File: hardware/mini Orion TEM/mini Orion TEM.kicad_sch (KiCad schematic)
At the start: 85 parts, among them J101 HRLV, J102 bridge to bottom board, J103 SWD, J104 fan pwr source, J105 VT harness, J106 fan PWR, J2 Fan enable, Q101 DI035P04PT, SW101 SW_DIP_x06, U101 ISOM8110DFS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

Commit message: instructions for dinguses
you know who
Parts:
- C101: value 1u -> 10u; mouser https://www.mouser.com/ProductDetail/Samsung-Electro-Mechanics/CL31B105KCHNNNE?qs=349EhDEZ59qH1i3RhF2lug%3D%3D -> https://www.mouser.com/ProductDetail/Samsung-Electro-Mechanics/CL31A106KBHNNNE?qs=sGAEpiMZZMsh%252B1woXyUXjxqcB7t9naYpzWmpMbMJIKQ%3D; specs 1uF, 100VDC, X7R, 10%, -55C, +125C -> 10uF, 50VDC, X5R, 10%, -55C, +85C; unit x1 0.15 -> (none); unit x10 0.061 -> 0.07
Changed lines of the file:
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@@
+	)
+	(symbol
+		(lib_id "Device:C_Small")
+		(at 73.66 39.37 0)
+		(unit 1)
+		(exclude_from_sim no)
+		(in_bom yes)
+		(on_board yes)
+		(dnp no)
+		(property "Reference" "C101"
+			(at 76.2 38.1062 0)
+			(effects
+				(font
+					(size 1.27 1.27)
+				)
+				(justify left)
+			)
+		)
+		(property "Value" "10u"
+			(at 76.2 40.6462 0)
+			(effects
+				(font
+					(size 1.27 1.27)
+				)
+				(justify left)
+			)
+		)
+		(property "Footprint" "Capacitor_SMD:C_1206_3216Metric_Pad1.33x1.80mm_HandSolder"
+			(at 73.66 39.37 0)
+			(effects
+				(font
+					(size 1.27 1.27)
+				)
+				(hide yes)
+			)
+		)
+		(property "Datasheet" ""
+			(at 73.66 39.37 0)
+			(effects
+				(font
+					(size 1.27 1.27)
+				)
+				(hide yes)
+			)
+		)
+		(property "Description" ""
+			(at 73.66 39.37 0)
+			(effects
+				(font
+					(size 1.27 1.27)
+				)
+				(hide yes)
+			)
+		)
+		(property "Sim.Device" ""
+			(at 73.66 39.37 0)
+			(effects
+				(font
+					(size 1.27 1.27)
+				)
+				(hide yes)
+			)
+		)
+		(property "Sim.Type" ""
+			(at 73.66 39.37 0)
+			(effects
+				(font
+					(size 1.27 1.27)
+				)
+				(hide yes)
+			)
+		)
+		(property "mouser" "https://www.mouser.com/ProductDetail/Samsung-Electro-Mechanics/CL31A106KBHNNNE?qs=sGAEpiMZZMsh%252B1woXyUXjxqcB7t9naYpzWmpMbMJIKQ%3D"
+			(at 73.66 39.37 0)
+			(effects
+				(font
+					(size 1.27 1.27)
+				)
+				(hide yes)
+			)
+		)
+		(property "specs" "10uF, 50VDC, X5R, 10%, -55C, +85C"
+			(at 73.66 39.37 0)
+			(effects
+				(font
+					(size 1.27 1.27)
+				)
+				(hide yes)
+			)
+		)
+		(property "unit x10" "0.07"
+			(at 73.66 39.37 0)
+			(effects
+				(font
+					(size 1.27 1.27)
+				)
+				(hide yes)
+			)
+		)
+		(property "Sim.Pins" ""
+			(at 73.66 39.37 0)
+			(effects
+				(font
+					(size 1.27 1.27)
+				)
+				(hide yes)
+			)
+		)
+		(property "note" ""
+			(at 73.66 39.37 0)
+			(effects
+				(font
+					(size 1.27 1.27)
+				)
+				(hide yes)
+			)
+		)
+		(pin "2"
+		)
+		(pin "1"
+		)
+		(instances
+			(project "mini Orion TEM"
+				(path "/b084770c-fa69-4b11-9ca5-6e8bd0701598"
+					(reference "C101")
+					(unit 1)
+				)
+			)
+		)
 	)
 	(symbol
@@
 					(unit 1)
 				)
-			)
-		)
-	)
-	(symbol
-		(lib_id "Device:C_Small")
-		(at 73.66 39.37 0)
-		(unit 1)
-		(exclude_from_sim no)
-		(in_bom yes)
-		(on_board yes)
-		(dnp no)
-		(property "Reference" "C101"
-			(at 76.2 38.1062 0)
-			(effects
-				(font
-					(size 1.27 1.27)
-				)
-				(justify left)
-			)
-		)
-		(property "Value" "1u"
-			(at 76.2 40.6462 0)
-			(effects
-				(font
-					(size 1.27 1.27)
-				)
-				(justify left)
-			)
-		)
-		(property "Footprint" "Capacitor_SMD:C_1206_3216Metric_Pad1.33x1.80mm_HandSolder"
-			(at 73.66 39.37 0)
-			(effects
-				(font
-					(size 1.27 1.27)
-				)
-				(hide yes)
-			)
-		)
-		(property "Datasheet" ""
-			(at 73.66 39.37 0)
-			(effects
-				(font
-					(size 1.27 1.27)
-				)
-				(hide yes)
-			)
-		)
-		(property "Description" ""
-			(at 73.66 39.37 0)
-			(effects
-				(font
-					(size 1.27 1.27)
-				)
-				(hide yes)
-			)
-		)
-		(property "Sim.Device" ""
-			(at 73.66 39.37 0)
-			(effects
-				(font
-					(size 1.27 1.27)
-				)
-				(hide yes)
-			)
-		)
-		(property "Sim.Type" ""
-			(at 73.66 39.37 0)
-			(effects
-				(font
-					(size 1.27 1.27)
-				)
-				(hide yes)
-			)
-		)
-		(property "mouser" "https://www.mouser.com/ProductDetail/Samsung-Electro-Mechanics/CL31B105KCHNNNE?qs=349EhDEZ59qH1i3RhF2lug%3D%3D"
-			(at 73.66 39.37 0)
-			(effects
-				(font
-					(size 1.27 1.27)
-				)
-				(hide yes)
-			)
-		)
-		(property "specs" "1uF, 100VDC, X7R, 10%, -55C, +125C"
-			(at 73.66 39.37 0)
-			(effects
-				(font
-					(size 1.27 1.27)
-				)
-				(hide yes)
-			)
-		)
-		(property "unit x10" "0.061"
-			(at 73.66 39.37 0)
-			(effects
-				(font
-					(size 1.27 1.27)
-				)
-				(hide yes)
-			)
-		)
-		(property "Sim.Pins" ""
-			(at 73.66 39.37 0)
-			(effects
-				(font
-					(size 1.27 1.27)
-				)
-				(hide yes)
-			)
-		)
-		(property "note" ""
-			(at 73.66 39.37 0)
-			(effects
-				(font
-					(size 1.27 1.27)
-				)
-				(hide yes)
-			)
-		)
-		(property "unit x1" "0.15"
-			(at 73.66 39.37 0)
-			(effects
-				(font
-					(size 1.27 1.27)
-				)
-				(hide yes)
-			)
-		)
-		(property "Mouser Part Number" ""
-			(at 73.66 39.37 0)
-			(effects
-				(font
-					(size 1.27 1.27)
-				)
-				(hide yes)
-			)
-		)
-		(pin "2"
-		)
-		(pin "1"
-		)
-		(instances
-			(project "mini Orion TEM"
-				(path "/b084770c-fa69-4b11-9ca5-6e8bd0701598"
-					(reference "C101")
-					(unit 1)
-				)

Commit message: rounder gooder
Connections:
- net HRLV_CAN+: now also FL101.4; no longer FL101.1
- net HRLV_CAN-: now also FL101.1; no longer FL101.4
- net at FL101.2: now also U104.5 (CANL); no longer U104.6 (CANH)
- net at FL101.3: now also U104.6 (CANH); no longer U104.5 (CANL)
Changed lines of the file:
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@@
 		(lib_id "Filter:Choke_CommonMode_FerriteCore_1243")
 		(at 104.14 54.61 0)
+		(mirror x)
 		(unit 1)
 		(exclude_from_sim no)
@@
 		(dnp no)
 		(property "Reference" "FL101"
-			(at 104.14 49.53 0)
+			(at 104.14 49.784 0)
 			(effects
 				(font
@@
 		)
 		(property "Value" "Choke_CommonMode_FerriteCore_1243"
-			(at 104.013 49.53 0)
+			(at 104.013 59.69 0)
 			(effects
 				(font
@@
 		)
 		(property "Footprint" "Inductor_SMD:L_CommonModeChoke_Coilcraft_1812CAN"
-			(at 104.14 60.96 0)
+			(at 104.14 48.26 0)
 			(effects
 				(font
@@
 		)
 		(property "Datasheet" "~"
-			(at 104.14 62.865 0)
+			(at 104.14 46.355 0)
 			(effects
 				(font
@@
 		)
 		(property "Description" "EMI 2-inductor common mode filter"
-			(at 108.204 55.372 0)
+			(at 108.204 53.848 0)
 			(effects
 				(font

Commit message: human part checker
always the part. never the part.
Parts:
- added Q102: MMBT5550L, Package_TO_SOT_SMD:SOT-23, symbol Transistor_BJT:MMBT5550L
- R113, R114: value 88.7k -> 40.2k; mouser https://www.mouser.com/ProductDetail/YAGEO/AC0805FR-0788K7L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 -> https://www.mouser.com/ProductDetail/KOA-Speer/RK73H2ATTD40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; specs 88.7kR, 125mW, 150V, 100ppm, 1%, -55C, +155C -> 40.2k ohm, 250mW, 1%, 150V, 100ppm, -55C, +155C; unit x1 0.01 -> 0.1; unit x10 0.011 -> 0.02
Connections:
- net +3V3: now also Q102.3 (C)
- net LV_FAN_PWM: now also Q102.1 (B); no longer R102.1
- new net: Q102.2 (E), R102.1
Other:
- note added: "join with external wire. see info.md in project folder"
- note added: "trust-me-bro technology"
- note removed: "join with external wire"
- moved on the sheet: C109, C110, C113, C114, R102

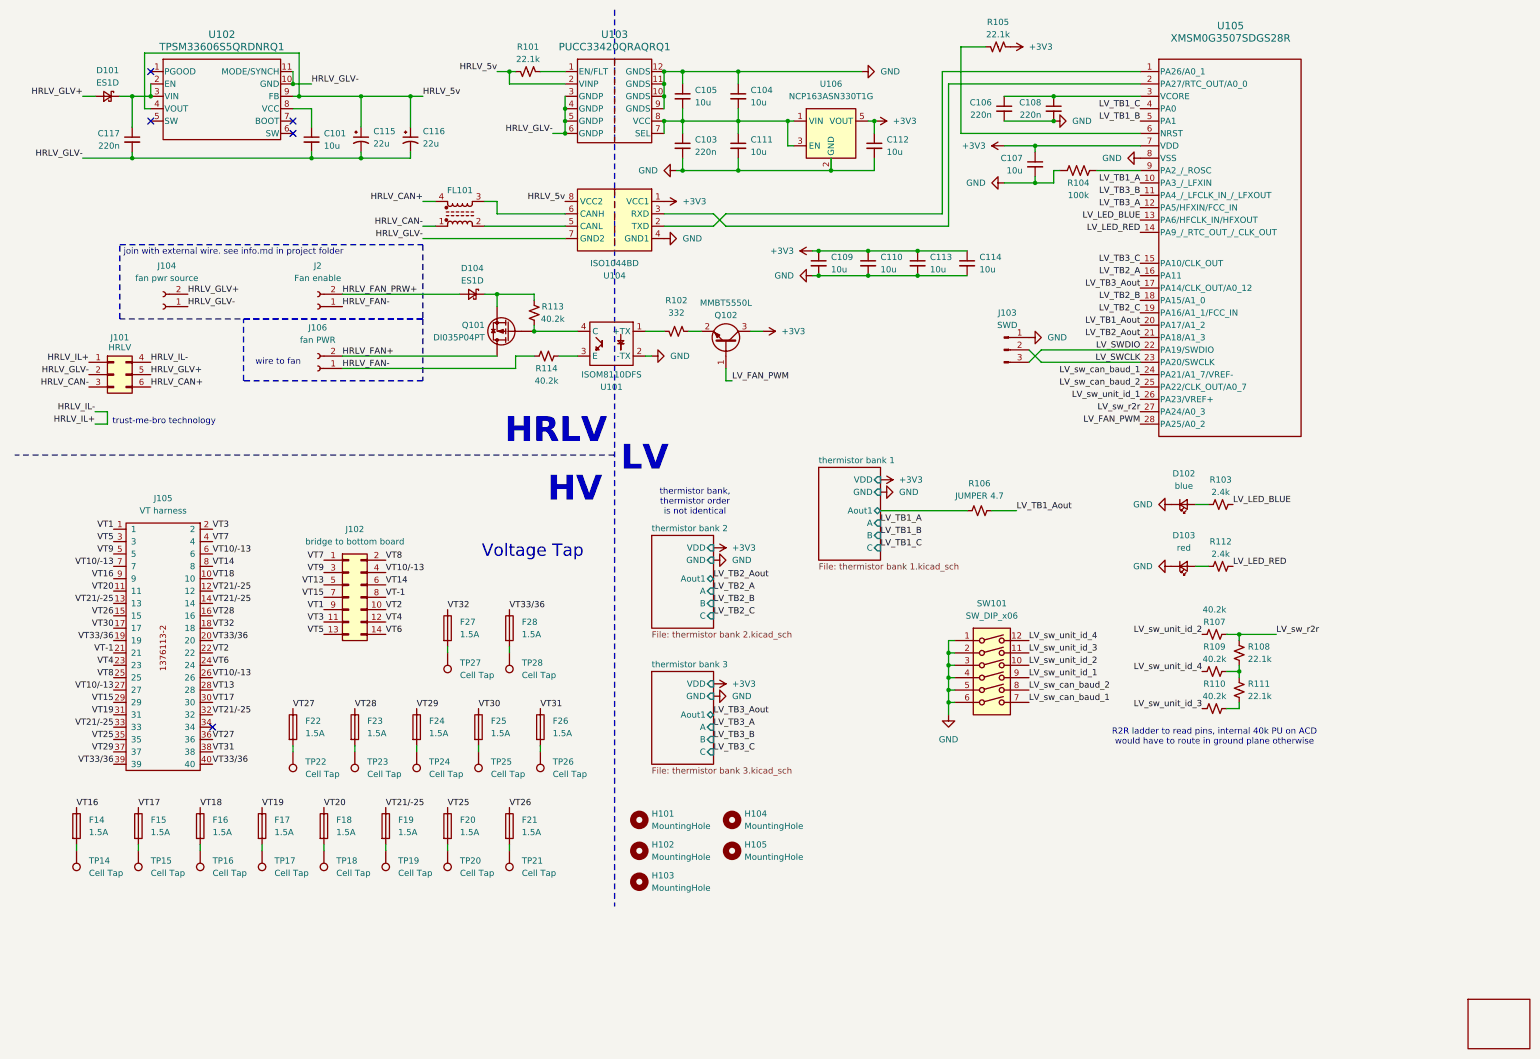
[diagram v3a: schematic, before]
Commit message: fixed silkscreen dissipearing
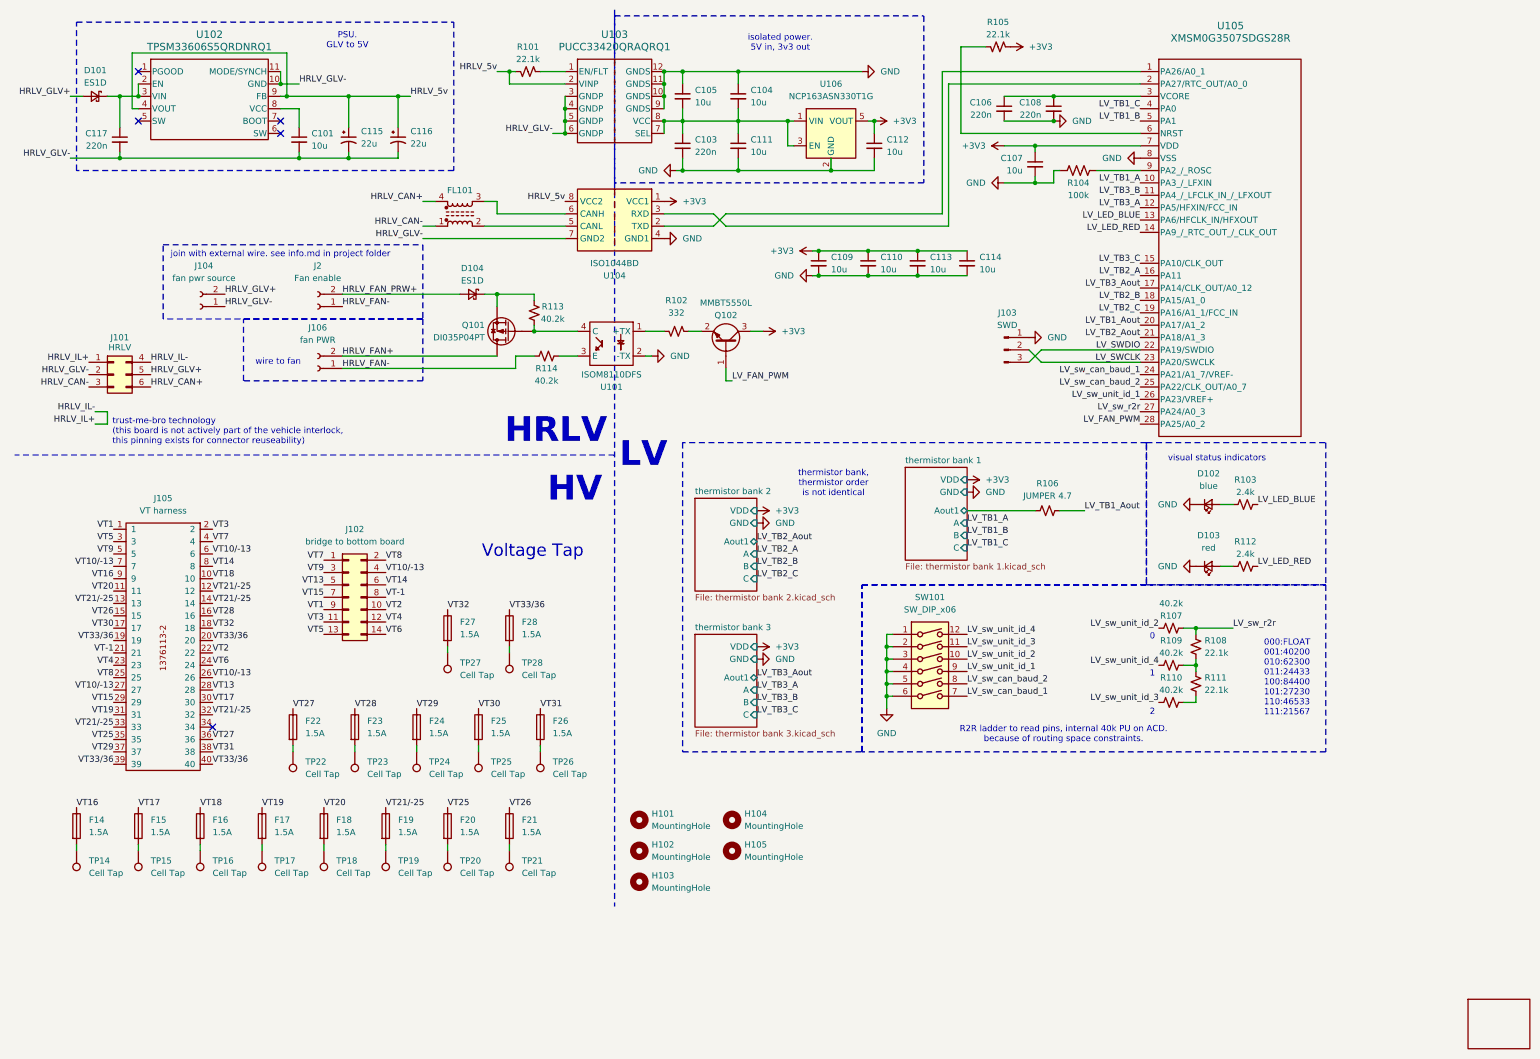
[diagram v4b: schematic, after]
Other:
- note added: "0"
- note added: "000:FLOAT 001:40200 010:62300 011:24433 100:84400 101:27230 110:46533 111:21567"
- note added: "1"
- note added: "2"
- note added: "PSU. GLV to 5V"
- note added: "R2R ladder to read pins, internal 40k PU on ACD. because of routing space constraints."
- note added: "isolated power. 5V in, 3v3 out"
- note added: "trust-me-bro technology (this board is not actively part of the vehicle interlock, this pinning exists for connector reuseability)"
- note added: "visual status indicators"
- note removed: "R2R ladder to read pins, internal 40k PU on ACD would have to route in ground plane otherwise"
- note removed: "trust-me-bro technology"
- moved on the sheet: C101, C115, C116, C117, D101, D102, D103, J104, R103, R106, R107, R108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

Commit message: maby
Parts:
- removed C115, C116: 22u, Capacitor_SMD:C_0805_2012Metric_Pad1.18x1.45mm_HandSolder, symbol Device:C_Polarized_Small_US
- added C115, C116: 22u, Capacitor_SMD:C_0805_2012Metric_Pad1.18x1.45mm_HandSolder, symbol Device:C_Small
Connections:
- net HRLV_5v: now also C115.1, C116.1
- net HRLV_GLV-: now also C115.2, C116.2
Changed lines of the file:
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@@
 	)
 	(symbol
+		(lib_id "Device:C_Small")
+		(at 81.28 39.37 0)
+		(unit 1)
+		(exclude_from_sim no)
+		(in_bom yes)
+		(on_board yes)
+		(dnp no)
+		(property "Reference" "C115"
+			(at 83.82 38.1062 0)
+			(effects
+				(font
+					(size 1.27 1.27)
+				)
+				(justify left)
+			)
+		)
+		(property "Value" "22u"
+			(at 83.82 40.6462 0)
+			(effects
+				(font
+					(size 1.27 1.27)
+				)
+				(justify left)
+			)
+		)
+		(property "Footprint" "Capacitor_SMD:C_0805_2012Metric_Pad1.18x1.45mm_HandSolder"
+			(at 81.28 39.37 0)
+			(effects
+				(font
+					(size 1.27 1.27)
+				)
+				(hide yes)
+			)
+		)
+		(property "Datasheet" ""
+			(at 81.28 39.37 0)
+			(effects
+				(font
+					(size 1.27 1.27)
+				)
+				(hide yes)
+			)
+		)
+		(property "Description" ""
+			(at 81.28 39.37 0)
+			(effects
+				(font
+					(size 1.27 1.27)
+				)
+				(hide yes)
+			)
+		)
+		(property "mouser" "https://www.mouser.com/ProductDetail/Samsung-Electro-Mechanics/CL21A226MAYNNNE?qs=sGAEpiMZZMsh%252B1woXyUXj9e2R%2FOkAO5o4FNiyGuFzx8%3D"
+			(at 81.28 39.37 0)
+			(effects
+				(font
+					(size 1.27 1.27)
+				)
+				(hide yes)
+			)
+		)
+		(property "specs" "22uF, 25V, 20%, X5R, -55C, +85C, mlcc"
+			(at 81.28 39.37 0)
+			(effects
+				(font
+					(size 1.27 1.27)
+				)
+				(hide yes)
+			)
+		)
+		(property "unit x10" "0.043"
+			(at 81.28 39.37 0)
+			(effects
+				(font
+					(size 1.27 1.27)
+				)
+				(hide yes)
+			)
+		)
+		(pin "2"
+		)
+		(pin "1"
+		)
+		(instances
+			(project "mini Orion TEM"
+				(path "/b084770c-fa69-4b11-9ca5-6e8bd0701598"
+					(reference "C115")
+					(unit 1)
+				)
+			)
+		)
+	)
+	(symbol
 		(lib_id "power:+3V3")
 		(at 217.17 20.32 270)
@@
 	)
 	(symbol
-		(lib_id "Device:C_Polarized_Small_US")
-		(at 91.44 39.37 0)
-		(unit 1)
-		(exclude_from_sim no)
-		(in_bom yes)
-		(on_board yes)
-		(dnp no)
-		(property "Reference" "C116"
-			(at 93.98 37.6681 0)
-			(effects
-				(font
-					(size 1.27 1.27)
-				)
-				(justify left)
-			)
-		)
-		(property "Value" "22u"
-			(at 93.98 40.2081 0)
-			(effects
-				(font
-					(size 1.27 1.27)
-				)
-				(justify left)
-			)
-		)
-		(property "Footprint" "Capacitor_SMD:C_0805_2012Metric_Pad1.18x1.45mm_HandSolder"
-			(at 91.44 39.37 0)
-			(effects
-				(font
-					(size 1.27 1.27)
-				)
-				(hide yes)
-			)
-		)
-		(property "Datasheet" "~"
-			(at 91.44 39.37 0)
-			(effects
-				(font
-					(size 1.27 1.27)
-				)
-				(hide yes)
-			)
-		)
-		(property "Description" "tantalium. 7v"
-			(at 91.44 39.37 0)
-			(effects
-				(font
-					(size 1.27 1.27)
-				)
-				(hide yes)
-			)
-		)
-		(property "mouser" "https://www.mouser.com/ProductDetail/Vishay-Sprague/TMCP0J226MTRF?qs=sGAEpiMZZMtZ1n0r9vR22SXwTtNEhYRLx5RUlLXY%252BB2j8IDJMMLmhQ%3D%3D"
-			(at 91.44 39.37 0)
-			(effects
-				(font
-					(size 1.27 1.27)
-				)
-				(hide yes)
-			)
-		)
-		(property "unit x1" ".33"
-			(at 91.44 39.37 0)
-			(effects
-				(font
-					(size 1.27 1.27)
-				)
-				(hide yes)
-			)
-		)
-		(property "unit x10" ".142"
-			(at 91.44 39.37 0)
-			(effects
-				(font
-					(size 1.27 1.27)
-				)
-				(hide yes)
-			)
-		)
-		(pin "2"
-		)
-		(pin "1"
-		)
-		(instances
-			(project "mini Orion TEM"
-				(path "/b084770c-fa69-4b11-9ca5-6e8bd0701598"
-					(reference "C116")
-					(unit 1)
-				)
-			)
-		)
-	)
-	(symbol
 		(lib_id "Connector:Conn_01x03_Pin")
 		(at 215.9 82.55 0)
@@
 	)
 	(symbol
-		(lib_id "Device:C_Polarized_Small_US")
-		(at 81.28 39.37 0)
-		(unit 1)
-		(exclude_from_sim no)
-		(in_bom yes)
-		(on_board yes)
-		(dnp no)
-		(fields_autoplaced yes)
-		(property "Reference" "C115"
-			(at 83.82 37.6681 0)
-			(effects
-				(font
-					(size 1.27 1.27)
-				)
-				(justify left)
-			)
-		)
-		(property "Value" "22u"
-			(at 83.82 40.2081 0)
-			(effects
-				(font
-					(size 1.27 1.27)
-				)
-				(justify left)
-			)
-		)
-		(property "Footprint" "Capacitor_SMD:C_0805_2012Metric_Pad1.18x1.45mm_HandSolder"
-			(at 81.28 39.37 0)
-			(effects
-				(font
-					(size 1.27 1.27)
-				)
-				(hide yes)
-			)
-		)
-		(property "Datasheet" "~"
-			(at 81.28 39.37 0)
-			(effects
-				(font
-					(size 1.27 1.27)
-				)
-				(hide yes)
-			)
-		)
-		(property "Description" "tantalium. 7v"
-			(at 81.28 39.37 0)
-			(effects
-				(font
-					(size 1.27 1.27)
-				)
-				(hide yes)
-			)
-		)
-		(property "mouser" "https://www.mouser.com/ProductDetail/Vishay-Sprague/TMCP0J226MTRF?qs=sGAEpiMZZMtZ1n0r9vR22SXwTtNEhYRLx5RUlLXY%252BB2j8IDJMMLmhQ%3D%3D"
-			(at 81.28 39.37 0)
-			(effects
-				(font
-					(size 1.27 1.27)
-				)
-				(hide yes)
-			)
-		)
-		(property "unit x1" ".33"
-			(at 81.28 39.37 0)
-			(effects
-				(font
-					(size 1.27 1.27)
-				)
-				(hide yes)
-			)
-		)
-		(property "unit x10" ".142"
-			(at 81.28 39.37 0)
-			(effects
-				(font
-					(size 1.27 1.27)
-				)
-				(hide yes)
-			)
-		)
-		(pin "2"
-		)
-		(pin "1"
-		)
-		(instances
-			(project ""
-				(path "/b084770c-fa69-4b11-9ca5-6e8bd0701598"
-					(reference "C115")
-					(unit 1)
-				)
-			)
-		)
-	)
-	(symbol
 		(lib_id "Transistor_BJT:MMBT5550L")
 		(at 158.75 81.28 270)
@@
 					(unit 1)
 				)
+			)
+		)
+	)
+	(symbol
+		(lib_id "Device:C_Small")
+		(at 91.44 39.37 0)
+		(unit 1)
+		(exclude_from_sim no)
+		(in_bom yes)
+		(on_board yes)
+		(dnp no)
+		(property "Reference" "C116"
+			(at 93.98 38.1062 0)
+			(effects
+				(font
+					(size 1.27 1.27)
+				)
+				(justify left)
+			)
+		)
+		(property "Value" "22u"
+			(at 93.98 40.6462 0)
+			(effects
+				(font
+					(size 1.27 1.27)
+				)
+				(justify left)
+			)
+		)
+		(property "Footprint" "Capacitor_SMD:C_0805_2012Metric_Pad1.18x1.45mm_HandSolder"
+			(at 91.44 39.37 0)
+			(effects
+				(font
+					(size 1.27 1.27)
+				)
+				(hide yes)
+			)
+		)
+		(property "Datasheet" ""
+			(at 91.44 39.37 0)
+			(effects
+				(font
+					(size 1.27 1.27)
+				)
+				(hide yes)
+			)
+		)
+		(property "Description" ""
+			(at 91.44 39.37 0)
+			(effects
+				(font
+					(size 1.27 1.27)
+				)
+				(hide yes)
+			)
+		)
+		(property "mouser" "https://www.mouser.com/ProductDetail/Samsung-Electro-Mechanics/CL21A226MAYNNNE?qs=sGAEpiMZZMsh%252B1woXyUXj9e2R%2FOkAO5o4FNiyGuFzx8%3D"
+			(at 91.44 39.37 0)
+			(effects
+				(font
+					(size 1.27 1.27)
+				)
+				(hide yes)
+			)
+		)
+		(property "specs" "22uF, 25V, 20%, X5R, -55C, +85C, mlcc"
+			(at 91.44 39.37 0)
+			(effects
+				(font
+					(size 1.27 1.27)
+				)
+				(hide yes)
+			)
+		)
+		(property "unit x10" "0.043"
+			(at 91.44 39.37 0)
+			(effects
+				(font
+					(size 1.27 1.27)
+				)
+				(hide yes)
+			)
+		)
+		(pin "2"
+		)
+		(pin "1"
+		)
+		(instances
+			(project "mini Orion TEM"
+				(path "/b084770c-fa69-4b11-9ca5-6e8bd0701598"
+					(reference "C116")
+					(unit 1)
+				)
